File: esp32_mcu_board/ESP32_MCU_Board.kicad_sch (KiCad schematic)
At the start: 4 parts, among them J1 Conn_01x10, J2 Conn_01x10, J3 Conn_01x19, J4 Conn_01x19

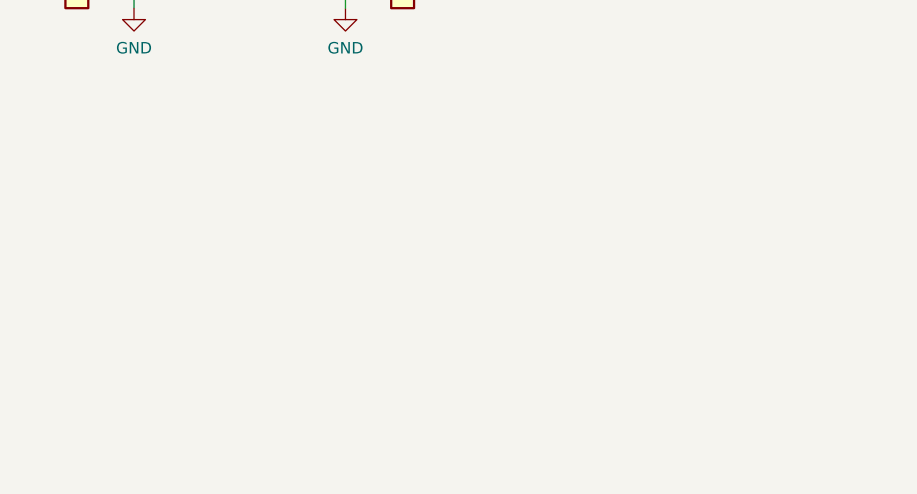
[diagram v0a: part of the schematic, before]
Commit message: Added ADS131M02IPWR ADC for MCU board to symbol and footprint library
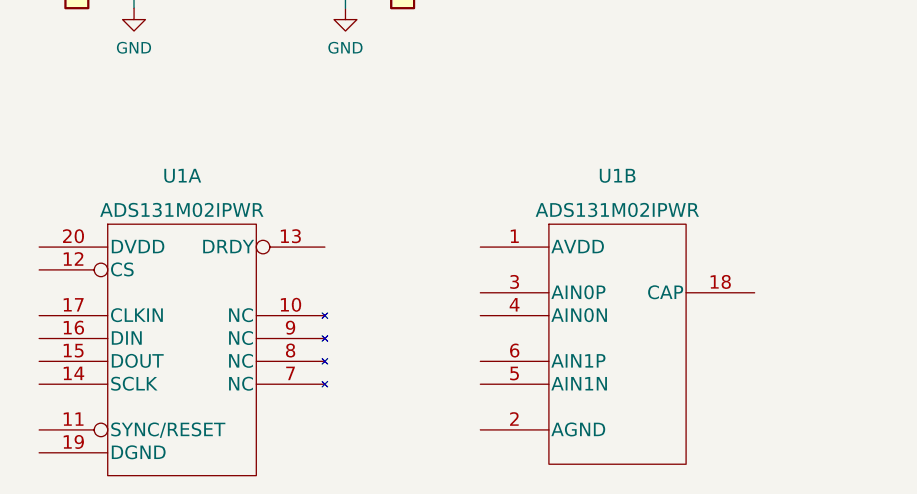
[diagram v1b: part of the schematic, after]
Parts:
- added U1: ADS131M02IPWR, footprints:ADS131M02IPWR, symbol ADS131M02:ADS131M02IPWR
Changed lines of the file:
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@@
     (pin "1")
+  )
+  (symbol (lib_name "ADS131M02IPWR_1") (lib_id "ADS131M02:ADS131M02IPWR") (at 14.224 89.408 0) (unit 1)
+    (in_bom yes) (on_board yes) (fields_autoplaced)
+    (property "Reference" "U1" (id 0) (at 45.339 80.264 0)
+      (effects (font (size 1.524 1.524)))
+    )
+    (property "Value" "ADS131M02IPWR" (id 1) (at 45.339 84.074 0)
+      (effects (font (size 1.524 1.524)))
+    )
+    (property "Footprint" "footprints:ADS131M02IPWR" (id 2) (at 45.974 113.538 0)
+      (effects (font (size 1.524 1.524)) hide)
+    )
+    (property "Datasheet" "" (id 3) (at 14.224 89.408 0)
+      (effects (font (size 1.524 1.524)))
+    )
+    (pin "10")
+    (pin "11")
+    (pin "12")
+    (pin "13")
+    (pin "14")
+    (pin "15")
+    (pin "16")
+    (pin "17")
+    (pin "19")
+    (pin "20")
+    (pin "7")
+    (pin "8")
+    (pin "9")
+    (pin "1")
+    (pin "18")
+    (pin "2")
+    (pin "3")
+    (pin "4")
+    (pin "5")
+    (pin "6")
   )
   (symbol (lib_id "Connector_Generic:Conn_01x19") (at 136.144 55.88 0) (unit 1)
@@
     (pin "9")
   )
+  (symbol (lib_id "ADS131M02:ADS131M02IPWR") (at 61.976 90.678 0) (unit 2)
+    (in_bom yes) (on_board yes) (fields_autoplaced)
+    (property "Reference" "U1" (id 0) (at 93.726 80.264 0)
+      (effects (font (size 1.524 1.524)))
+    )
+    (property "Value" "ADS131M02IPWR" (id 1) (at 93.726 84.074 0)
+      (effects (font (size 1.524 1.524)))
+    )
+    (property "Footprint" "footprints:ADS131M02IPWR" (id 2) (at 93.726 114.808 0)
+      (effects (font (size 1.524 1.524)) hide)
+    )
+    (property "Datasheet" "" (id 3) (at 61.976 90.678 0)
+      (effects (font (size 1.524 1.524)))
+    )
+    (pin "10")
+    (pin "11")
+    (pin "12")
+    (pin "13")
+    (pin "14")
+    (pin "15")
+    (pin "16")
+    (pin "17")
+    (pin "19")
+    (pin "20")
+    (pin "7")
+    (pin "8")
+    (pin "9")
+    (pin "1")
+    (pin "18")
+    (pin "2")
+    (pin "3")
+    (pin "4")
+    (pin "5")
+    (pin "6")
+  )
   (sheet_instances
     (path "/" (page "1"))
@@
       (reference "J4") (unit 1) (value "Conn_01x19") (footprint "Connector_PinSocket_2.54mm:PinSocket_1x19_P2.54mm_Vertical")
     )
+    (path "/cf9b2515-2215-4ee3-803a-a17b14ca6f8f"
+      (reference "U1") (unit 1) (value "ADS131M02IPWR") (footprint "footprints:ADS131M02IPWR")
+    )
+    (path "/e94af37f-6049-44e9-b4de-caa6c9032b51"
+      (reference "U1") (unit 2) (value "ADS131M02IPWR") (footprint "footprints:ADS131M02IPWR")
+    )
   )
